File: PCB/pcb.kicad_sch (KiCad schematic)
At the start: 220 parts

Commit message: Added LEDs to the Schematic
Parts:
- added D? (x100): SK6812MINI, LED_SMD:LED_SK6812MINI_PLCC4_3.5x3.5mm_P1.75mm, symbol LED:SK6812MINI
- C1: value (none) -> 10u; footprint (none) -> Capacitor_SMD:C_0805_2012Metric
- C2, C3, C4: value (none) -> 0.1uF; footprint (none) -> Capacitor_SMD:C_0805_2012Metric
- C5, C6: value (none) -> 22pF; footprint (none) -> Capacitor_SMD:C_0805_2012Metric
- C7: value (none) -> 10uF; footprint (none) -> Capacitor_SMD:C_0805_2012Metric
- C8: value (none) -> 1uF; footprint (none) -> Capacitor_SMD:C_0805_2012Metric
- D1: value (none) -> Esc; footprint (none) -> Diode_SMD:D_SOD-123
- D10: value (none) -> <; footprint (none) -> Diode_SMD:D_SOD-123
- D100, D74: value (none) -> Enter; footprint (none) -> Diode_SMD:D_SOD-123
- D11, D71: value (none) -> Win; footprint (none) -> Diode_SMD:D_SOD-123
- D12: value (none) -> F1; footprint (none) -> Diode_SMD:D_SOD-123
- D13, D92: value (none) -> 2; footprint (none) -> Diode_SMD:D_SOD-123
- D14: value (none) -> W; footprint (none) -> Diode_SMD:D_SOD-123
- D15: value (none) -> S; footprint (none) -> Diode_SMD:D_SOD-123
- D16: value (none) -> Y; footprint (none) -> Diode_SMD:D_SOD-123
- D17: value (none) -> Alt; footprint (none) -> Diode_SMD:D_SOD-123
- D18: value (none) -> F2; footprint (none) -> Diode_SMD:D_SOD-123
- D19, D97: value (none) -> 3; footprint (none) -> Diode_SMD:D_SOD-123
- D2: value (none) -> ^; footprint (none) -> Diode_SMD:D_SOD-123
- D20: value (none) -> E; footprint (none) -> Diode_SMD:D_SOD-123
- D21: value (none) -> D; footprint (none) -> Diode_SMD:D_SOD-123
- D22: value (none) -> X; footprint (none) -> Diode_SMD:D_SOD-123
- D23: value (none) -> F3; footprint (none) -> Diode_SMD:D_SOD-123
- D24, D86: value (none) -> 4; footprint (none) -> Diode_SMD:D_SOD-123
- D25: value (none) -> R; footprint (none) -> Diode_SMD:D_SOD-123
- D26: value (none) -> F; footprint (none) -> Diode_SMD:D_SOD-123
- D27: value (none) -> C; footprint (none) -> Diode_SMD:D_SOD-123
- D28: value (none) -> F4; footprint (none) -> Diode_SMD:D_SOD-123
- D29, D91: value (none) -> 5; footprint (none) -> Diode_SMD:D_SOD-123
- D3: value (none) -> Tab; footprint (none) -> Diode_SMD:D_SOD-123
- D30: value (none) -> T; footprint (none) -> Diode_SMD:D_SOD-123
- D31: value (none) -> G; footprint (none) -> Diode_SMD:D_SOD-123
- D32: value (none) -> V; footprint (none) -> Diode_SMD:D_SOD-123
- D33: value (none) -> F5; footprint (none) -> Diode_SMD:D_SOD-123
- D34, D96: value (none) -> 6; footprint (none) -> Diode_SMD:D_SOD-123
- D35: value (none) -> Z; footprint (none) -> Diode_SMD:D_SOD-123
- D36: value (none) -> H; footprint (none) -> Diode_SMD:D_SOD-123
- D37: value (none) -> B; footprint (none) -> Diode_SMD:D_SOD-123
- D38: value (none) -> Leer; footprint (none) -> Diode_SMD:D_SOD-123
- D39: value (none) -> F6; footprint (none) -> Diode_SMD:D_SOD-123
- D4: value (none) -> Caps; footprint (none) -> Diode_SMD:D_SOD-123
- D40, D85: value (none) -> 7; footprint (none) -> Diode_SMD:D_SOD-123
- D41: value (none) -> U; footprint (none) -> Diode_SMD:D_SOD-123
- D42: value (none) -> J; footprint (none) -> Diode_SMD:D_SOD-123
- D43: value (none) -> N; footprint (none) -> Diode_SMD:D_SOD-123
- D44: value (none) -> F7; footprint (none) -> Diode_SMD:D_SOD-123
- D45, D90: value (none) -> 8; footprint (none) -> Diode_SMD:D_SOD-123
- D46: value (none) -> I; footprint (none) -> Diode_SMD:D_SOD-123
- D47: value (none) -> K; footprint (none) -> Diode_SMD:D_SOD-123
- D48: value (none) -> M; footprint (none) -> Diode_SMD:D_SOD-123
- D49: value (none) -> F8; footprint (none) -> Diode_SMD:D_SOD-123
- D5, D70: value (none) -> Shift; footprint (none) -> Diode_SMD:D_SOD-123
- D50, D95: value (none) -> 9; footprint (none) -> Diode_SMD:D_SOD-123
- D51: value (none) -> O; footprint (none) -> Diode_SMD:D_SOD-123
- D52: value (none) -> L; footprint (none) -> Diode_SMD:D_SOD-123
- D53, D93: value (none) -> ,; footprint (none) -> Diode_SMD:D_SOD-123
- D54: value (none) -> F9; footprint (none) -> Diode_SMD:D_SOD-123
- D55, D88: value (none) -> 0; footprint (none) -> Diode_SMD:D_SOD-123
- D56: value (none) -> P; footprint (none) -> Diode_SMD:D_SOD-123
- D57: value (none) -> Ö; footprint (none) -> Diode_SMD:D_SOD-123
- D58: value (none) -> .; footprint (none) -> Diode_SMD:D_SOD-123
- D59: value (none) -> AltGr; footprint (none) -> Diode_SMD:D_SOD-123
- D6: value (none) -> Ctrl; footprint (none) -> Diode_SMD:D_SOD-123
- D60: value (none) -> F10; footprint (none) -> Diode_SMD:D_SOD-123
- D61: value (none) -> ß; footprint (none) -> Diode_SMD:D_SOD-123
- D62: value (none) -> Ü; footprint (none) -> Diode_SMD:D_SOD-123
- D63: value (none) -> Ä; footprint (none) -> Diode_SMD:D_SOD-123
- D64, D98: value (none) -> -; footprint (none) -> Diode_SMD:D_SOD-123
- D65: value (none) -> Fn; footprint (none) -> Diode_SMD:D_SOD-123
- D66: value (none) -> F11; footprint (none) -> Diode_SMD:D_SOD-123
- D67: value (none) -> ´; footprint (none) -> Diode_SMD:D_SOD-123
- D68, D99: value (none) -> +; footprint (none) -> Diode_SMD:D_SOD-123
- D69: value (none) -> #; footprint (none) -> Diode_SMD:D_SOD-123
- D7, D87: value (none) -> 1; footprint (none) -> Diode_SMD:D_SOD-123
- D72: value (none) -> F12; footprint (none) -> Diode_SMD:D_SOD-123
- D73: value (none) -> Back; footprint (none) -> Diode_SMD:D_SOD-123
- D75: value (none) -> Left; footprint (none) -> Diode_SMD:D_SOD-123
- D76: value (none) -> Up; footprint (none) -> Diode_SMD:D_SOD-123
- D77: value (none) -> Down; footprint (none) -> Diode_SMD:D_SOD-123
- D78: value (none) -> Right; footprint (none) -> Diode_SMD:D_SOD-123
- D79: value (none) -> Druck; footprint (none) -> Diode_SMD:D_SOD-123
- D8: value (none) -> Q; footprint (none) -> Diode_SMD:D_SOD-123
- D80: value (none) -> Insert; footprint (none) -> Diode_SMD:D_SOD-123
- D81: value (none) -> Del; footprint (none) -> Diode_SMD:D_SOD-123
- D82: value (none) -> PgUp; footprint (none) -> Diode_SMD:D_SOD-123
- D83: value (none) -> PgDn; footprint (none) -> Diode_SMD:D_SOD-123
- D84: value (none) -> NumLock; footprint (none) -> Diode_SMD:D_SOD-123
- D89: value (none) -> /; footprint (none) -> Diode_SMD:D_SOD-123
- D9: value (none) -> A; footprint (none) -> Diode_SMD:D_SOD-123
- D94: value (none) -> *; footprint (none) -> Diode_SMD:D_SOD-123
- F1: value (none) -> 500mA; footprint (none) -> Fuse:Fuse_1206_3216Metric
- FB1: value (none) -> 600R; footprint (none) -> Ferrite_THT:LairdTech_28C0236-0JW-10
- J1: value (none) -> USB_C_Receptacle_USB2.0; footprint (none) -> Connector_USB:USB_C_Receptacle_HRO_TYPE-C-31-M-12
- MX? (x100): value (none) -> MX-NoLED
- R1, R2: value (none) -> 5K1; footprint (none) -> Resistor_SMD:R_0805_2012Metric
- R3, R4: value (none) -> 22; footprint (none) -> Resistor_SMD:R_0805_2012Metric
- R5, R6: value (none) -> 10k; footprint (none) -> Resistor_SMD:R_0805_2012Metric
- SW1: value (none) -> SW_Push; footprint (none) -> random-keyboard-parts:SKQG-1155865
- U1: value (none) -> AT90USB1286-AU; footprint (none) -> Package_QFP:TQFP-64_14x14mm_P0.8mm
- Y1: value (none) -> Crystal_GND24_Small; footprint (none) -> Crystal:Crystal_SMD_3225-4Pin_3.2x2.5mm
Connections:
- net +5V: now also D?.4 (VDD), D?.4 (VDD), D?.4 (VDD), D?.4 (VDD), D?.4 (VDD), D?.4 (VDD), D?.4 (VDD), D?.4 (VDD), D?.4 (VDD), D?.4 (VDD), D?.4 (VDD), D?.4 (VDD), D?.4 (VDD), D?.4 (VDD), D?.4 (VDD), D?.4 (VDD), D?.4 (VDD), D?.4 (VDD), D?.4 (VDD), D?.4 (VDD), D?.4 (VDD), D?.4 (VDD), D?.4 (VDD), D?.4 (VDD), D?.4 (VDD), D?.4 (VDD), D?.4 (VDD), D?.4 (VDD), D?.4 (VDD), D?.4 (VDD), D?.4 (VDD), D?.4 (VDD), D?.4 (VDD), D?.4 (VDD), D?.4 (VDD), D?.4 (VDD), D?.4 (VDD), D?.4 (VDD), D?.4 (VDD), D?.4 (VDD), D?.4 (VDD), D?.4 (VDD), D?.4 (VDD), D?.4 (VDD), D?.4 (VDD), D?.4 (VDD), D?.4 (VDD), D?.4 (VDD), D?.4 (VDD), D?.4 (VDD), D?.4 (VDD), D?.4 (VDD), D?.4 (VDD), D?.4 (VDD), D?.4 (VDD), D?.4 (VDD), D?.4 (VDD), D?.4 (VDD), D?.4 (VDD), D?.4 (VDD), D?.4 (VDD), D?.4 (VDD), D?.4 (VDD), D?.4 (VDD), D?.4 (VDD), D?.4 (VDD), D?.4 (VDD), D?.4 (VDD), D?.4 (VDD), D?.4 (VDD), D?.4 (VDD), D?.4 (VDD), D?.4 (VDD), D?.4 (VDD), D?.4 (VDD), D?.4 (VDD), D?.4 (VDD), D?.4 (VDD), D?.4 (VDD), D?.4 (VDD), D?.4 (VDD), D?.4 (VDD), D?.4 (VDD), D?.4 (VDD), D?.4 (VDD), D?.4 (VDD), D?.4 (VDD), D?.4 (VDD), D?.4 (VDD), D?.4 (VDD), D?.4 (VDD), D?.4 (VDD), D?.4 (VDD), D?.4 (VDD), D?.4 (VDD), D?.4 (VDD), D?.4 (VDD), D?.4 (VDD), D?.4 (VDD), D?.4 (VDD)
- net GND: now also D?.2 (VSS), D?.2 (VSS), D?.2 (VSS), D?.2 (VSS), D?.2 (VSS), D?.2 (VSS), D?.2 (VSS), D?.2 (VSS), D?.2 (VSS), D?.2 (VSS), D?.2 (VSS), D?.2 (VSS), D?.2 (VSS), D?.2 (VSS), D?.2 (VSS), D?.2 (VSS), D?.2 (VSS), D?.2 (VSS), D?.2 (VSS), D?.2 (VSS), D?.2 (VSS), D?.2 (VSS), D?.2 (VSS), D?.2 (VSS), D?.2 (VSS), D?.2 (VSS), D?.2 (VSS), D?.2 (VSS), D?.2 (VSS), D?.2 (VSS), D?.2 (VSS), D?.2 (VSS), D?.2 (VSS), D?.2 (VSS), D?.2 (VSS), D?.2 (VSS), D?.2 (VSS), D?.2 (VSS), D?.2 (VSS), D?.2 (VSS), D?.2 (VSS), D?.2 (VSS), D?.2 (VSS), D?.2 (VSS), D?.2 (VSS), D?.2 (VSS), D?.2 (VSS), D?.2 (VSS), D?.2 (VSS), D?.2 (VSS), D?.2 (VSS), D?.2 (VSS), D?.2 (VSS), D?.2 (VSS), D?.2 (VSS), D?.2 (VSS), D?.2 (VSS), D?.2 (VSS), D?.2 (VSS), D?.2 (VSS), D?.2 (VSS), D?.2 (VSS), D?.2 (VSS), D?.2 (VSS), D?.2 (VSS), D?.2 (VSS), D?.2 (VSS), D?.2 (VSS), D?.2 (VSS), D?.2 (VSS), D?.2 (VSS), D?.2 (VSS), D?.2 (VSS), D?.2 (VSS), D?.2 (VSS), D?.2 (VSS), D?.2 (VSS), D?.2 (VSS), D?.2 (VSS), D?.2 (VSS), D?.2 (VSS), D?.2 (VSS), D?.2 (VSS), D?.2 (VSS), D?.2 (VSS), D?.2 (VSS), D?.2 (VSS), D?.2 (VSS), D?.2 (VSS), D?.2 (VSS), D?.2 (VSS), D?.2 (VSS), D?.2 (VSS), D?.2 (VSS), D?.2 (VSS), D?.2 (VSS), D?.2 (VSS), D?.2 (VSS), D?.2 (VSS), D?.2 (VSS)
- new net: D?.1 (DOUT), D?.3 (DIN) (x90)
- new net RGBDIN: D?.3 (DIN)
- new net RGBDOUT0: D?.1 (DOUT), D?.3 (DIN)
- new net RGBDOUT1: D?.1 (DOUT), D?.3 (DIN)
- new net RGBDOUT2: D?.1 (DOUT), D?.3 (DIN)
- new net RGBDOUT3: D?.1 (DOUT), D?.3 (DIN)
- new net RGBDOUT4: D?.1 (DOUT), D?.3 (DIN)
- new net RGBDOUT5: D?.1 (DOUT), D?.3 (DIN)
- new net RGBDOUT6: D?.1 (DOUT), D?.3 (DIN)
- new net RGBDOUT7: D?.1 (DOUT), D?.3 (DIN)
- new net RGBDOUT8: D?.1 (DOUT), D?.3 (DIN)
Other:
- company: (none) -> DiomKBS
- title: (none) -> Diom-75TK
- moved on the sheet: D1, D10, D100, D11, D12, D13, D14, D15, D16, D17, D18, D19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

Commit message: Submodule, LEDs, Footprints
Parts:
- MX1, MX10, MX12, MX13, MX14, MX15, MX16, MX18, MX19, MX2, MX20, MX21, MX22, MX23, MX24, MX25, MX26, MX27, MX28, MX29, MX30, MX31, MX32, MX33, MX34, MX35, MX36, MX37, MX39, MX40, MX41, MX42, MX43, MX44, MX45, MX46, MX47, MX48, MX49, MX50, MX51, MX52, MX53, MX54, MX55, MX56, MX57, MX58, MX60, MX61, MX62, MX63, MX64, MX65, MX66, MX67, MX68, MX69, MX7, MX71, MX72, MX75, MX76, MX77, MX78, MX79, MX8, MX80, MX81, MX82, MX83, MX84, MX85, MX86, MX87, MX89, MX9, MX90, MX91, MX92, MX93, MX94, MX95, MX96, MX97, MX98: renamed from MX?; footprint (none) -> MX_Alps_Hybrid:MX-1U-NoLED
- MX11, MX17, MX5, MX59, MX6: renamed from MX?; footprint (none) -> MX_Alps_Hybrid:MX-1.25U-NoLED
- MX3: renamed from MX?; footprint (none) -> MX_Alps_Hybrid:MX-1.5U-NoLED
- MX38: renamed from MX?; footprint (none) -> MX_Alps_Hybrid:MX-6U-Centered-NoLED
- MX4, MX70: renamed from MX?; footprint (none) -> MX_Alps_Hybrid:MX-1.75U-NoLED
- MX73, MX88: renamed from MX?; footprint (none) -> MX_Alps_Hybrid:MX-2U-NoLED
- gave numbers to parts that had none: 103

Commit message: Started PCB + Changed Footprints
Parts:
- D101, D102, D103, D104, D105, D106, D107, D108, D109, D110, D111, D112, D113, D114, D115, D116, D117, D118, D119, D120, D121, D122, D123, D124, D125, D126, D127, D128, D129, D130, D131, D132, D133, D134, D135, D136, D137, D138, D139, D140, D141, D142, D143, D144, D145, D146, D147, D148, D149, D150, D151, D152, D153, D154, D155, D156, D157, D158, D159, D160, D161, D162, D163, D164, D165, D166, D167, D168, D169, D170, D171, D172, D173, D174, D175, D176, D177, D178, D179, D180, D181, D182, D183, D184, D185, D186, D187, D188, D189, D190, D191, D192, D193, D194, D195, D196, D197, D198, D199, D200: footprint LED_SMD:LED_SK6812MINI_PLCC4_3.5x3.5mm_P1.75mm -> (none)
- MX1, MX10, MX12, MX13, MX14, MX15, MX16, MX18, MX19, MX2, MX20, MX21, MX22, MX23, MX24, MX25, MX26, MX27, MX28, MX29, MX30, MX31, MX32, MX33, MX34, MX35, MX36, MX37, MX39, MX40, MX41, MX42, MX43, MX44, MX45, MX46, MX47, MX48, MX49, MX50, MX51, MX52, MX53, MX54, MX55, MX56, MX57, MX58, MX60, MX61, MX62, MX63, MX64, MX65, MX66, MX67, MX68, MX69, MX7, MX71, MX72, MX75, MX76, MX77, MX78, MX79, MX8, MX80, MX81, MX82, MX83, MX84, MX85, MX86, MX87, MX89, MX9, MX90, MX91, MX92, MX93, MX94, MX95, MX96, MX97, MX98: footprint MX_Alps_Hybrid:MX-1U-NoLED -> (none)
- MX11, MX17, MX5, MX59, MX6: footprint MX_Alps_Hybrid:MX-1.25U-NoLED -> (none)
- MX3: footprint MX_Alps_Hybrid:MX-1.5U-NoLED -> (none)
- MX38: footprint MX_Alps_Hybrid:MX-6U-Centered-NoLED -> (none)
- MX4, MX70: footprint MX_Alps_Hybrid:MX-1.75U-NoLED -> (none)
- MX73, MX88: footprint MX_Alps_Hybrid:MX-2U-NoLED -> (none)

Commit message: Finished Switch Layout
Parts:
- D101, D102, D103, D104, D105, D106, D107, D108, D109, D110, D111, D112, D113, D114, D115, D116, D117, D118, D119, D120, D121, D122, D123, D124, D125, D126, D127, D128, D129, D130, D131, D132, D133, D134, D135, D136, D137, D138, D139, D140, D141, D142, D143, D144, D145, D146, D147, D148, D149, D150, D151, D152, D153, D154, D155, D156, D157, D158, D159, D160, D161, D162, D163, D164, D165, D166, D167, D168, D169, D170, D171, D172, D173, D174, D175, D176, D177, D178, D179, D180, D181, D182, D183, D184, D185, D186, D187, D188, D189, D190, D191, D192, D193, D194, D195, D196, D197, D198, D199, D200: footprint (none) -> led:SK6812MINI_3.5x3.7mm_SMD
- MX1, MX10, MX12, MX13, MX14, MX15, MX16, MX18, MX19, MX2, MX20, MX21, MX22, MX23, MX24, MX25, MX26, MX27, MX28, MX29, MX30, MX31, MX32, MX33, MX34, MX35, MX36, MX37, MX39, MX40, MX41, MX42, MX43, MX44, MX45, MX46, MX47, MX48, MX49, MX50, MX51, MX52, MX53, MX54, MX55, MX56, MX57, MX58, MX60, MX61, MX62, MX63, MX64, MX65, MX66, MX67, MX68, MX69, MX7, MX71, MX72, MX75, MX76, MX77, MX78, MX79, MX8, MX80, MX81, MX82, MX83, MX84, MX85, MX86, MX87, MX89, MX9, MX90, MX91, MX92, MX93, MX94, MX95, MX96, MX97, MX98: footprint (none) -> kailh-switches-hotswap:Kailh-Hotswap-1U
- MX100, MX99: footprint (none) -> kailh-switches-hotswap:Kailh-Hotswap-2U-Vertical
- MX11, MX17, MX5, MX59, MX6: footprint (none) -> kailh-switches-hotswap:Kailh-Hotswap-1.25U
- MX3: footprint (none) -> kailh-switches-hotswap:Kailh-Hotswap-1.5U
- MX38: footprint (none) -> kailh-switches-hotswap:Kailh-Hotswap-6U
- MX4: footprint (none) -> kailh-switches-hotswap:Kailh-Hotswap-1.75U
- MX73, MX88: footprint (none) -> kailh-switches-hotswap:Kailh-Hotswap-2U
- MX74: footprint (none) -> kailh-switches-hotswap:Kailh-Hotswap-EnterISO

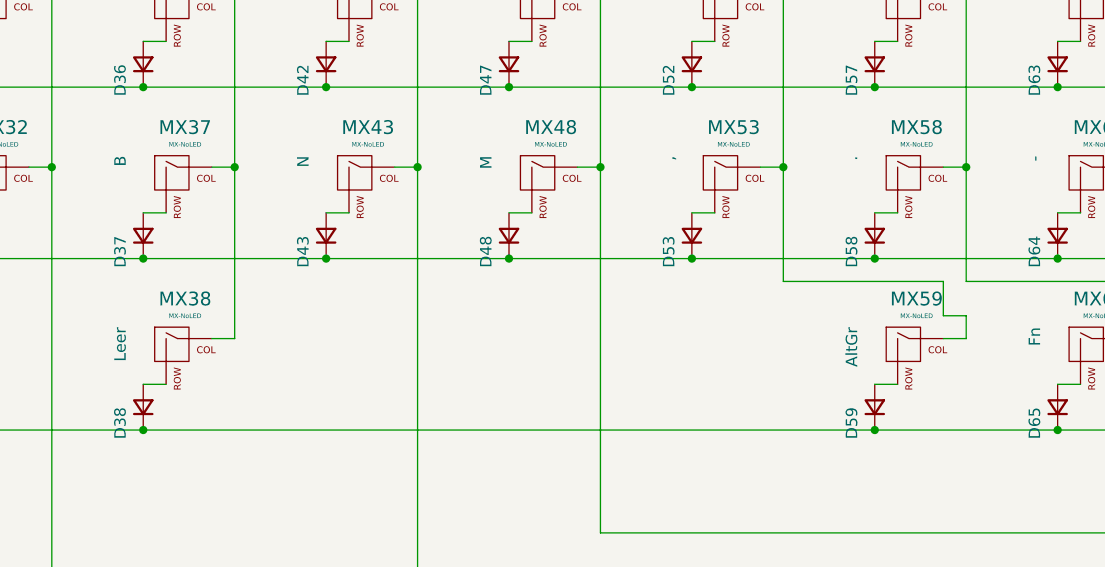
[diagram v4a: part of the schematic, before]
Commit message: Diode placement, Alternative Bottom Rows
-New Footprints
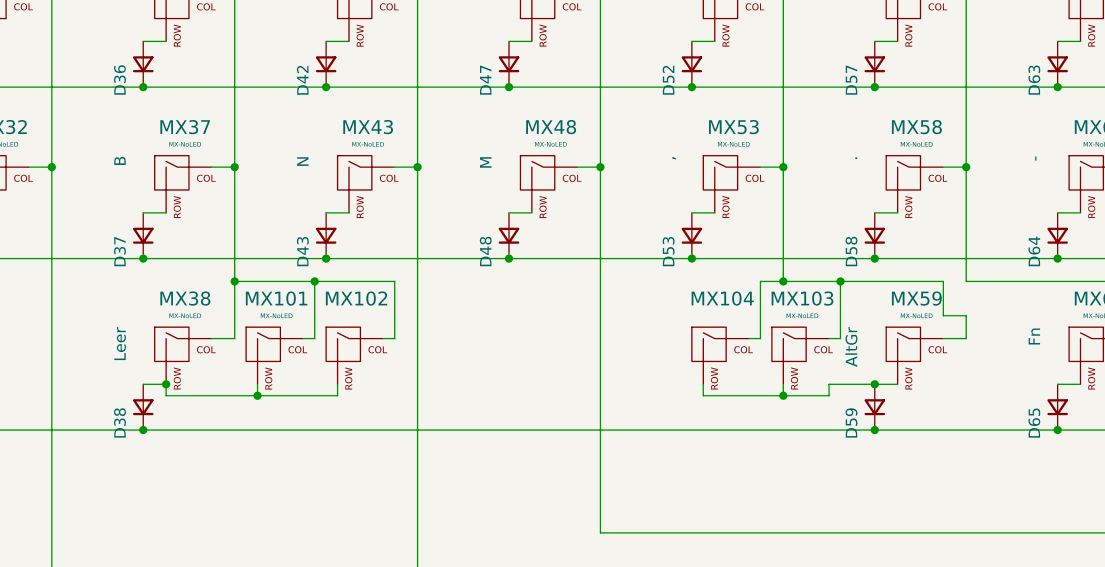
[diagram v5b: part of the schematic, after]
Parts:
- added MX101, MX103: MX-NoLED, symbol pcb-rescue:MX-NoLED-MX_Alps_Hybrid
- added MX102, MX104: (no value), symbol pcb-rescue:MX-NoLED-MX_Alps_Hybrid
- MX1, MX10, MX12, MX13, MX14, MX15, MX16, MX18, MX19, MX2, MX20, MX21, MX22, MX23, MX24, MX25, MX26, MX27, MX28, MX29, MX30, MX31, MX32, MX33, MX34, MX35, MX36, MX37, MX39, MX40, MX41, MX42, MX43, MX44, MX45, MX46, MX47, MX48, MX49, MX50, MX51, MX52, MX53, MX54, MX55, MX56, MX57, MX58, MX60, MX61, MX62, MX63, MX64, MX65, MX66, MX67, MX68, MX69, MX7, MX71, MX72, MX75, MX76, MX77, MX78, MX79, MX8, MX80, MX81, MX82, MX83, MX84, MX85, MX86, MX87, MX89, MX9, MX90, MX91, MX92, MX93, MX94, MX95, MX96, MX97, MX98: footprint kailh-switches-hotswap:Kailh-Hotswap-1U -> (none)
- MX100, MX99: footprint kailh-switches-hotswap:Kailh-Hotswap-2U-Vertical -> (none)
- MX11, MX17, MX5, MX59, MX6: footprint kailh-switches-hotswap:Kailh-Hotswap-1.25U -> (none)
- MX3: footprint kailh-switches-hotswap:Kailh-Hotswap-1.5U -> (none)
- MX38: footprint kailh-switches-hotswap:Kailh-Hotswap-6U -> (none)
- MX4: footprint kailh-switches-hotswap:Kailh-Hotswap-1.75U -> (none)
- MX73, MX88: footprint kailh-switches-hotswap:Kailh-Hotswap-2U -> (none)
- MX74: footprint kailh-switches-hotswap:Kailh-Hotswap-EnterISO -> (none)
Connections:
- net COL6: now also MX101.1 (COL), MX102.1 (COL)
- net COL9: now also MX103.1 (COL), MX104.1 (COL)
- net at D59.2 (A), MX59.2 (ROW): now also MX103.2 (ROW), MX104.2 (ROW)
- net at D38.2 (A), MX38.2 (ROW): now also MX101.2 (ROW), MX102.2 (ROW)

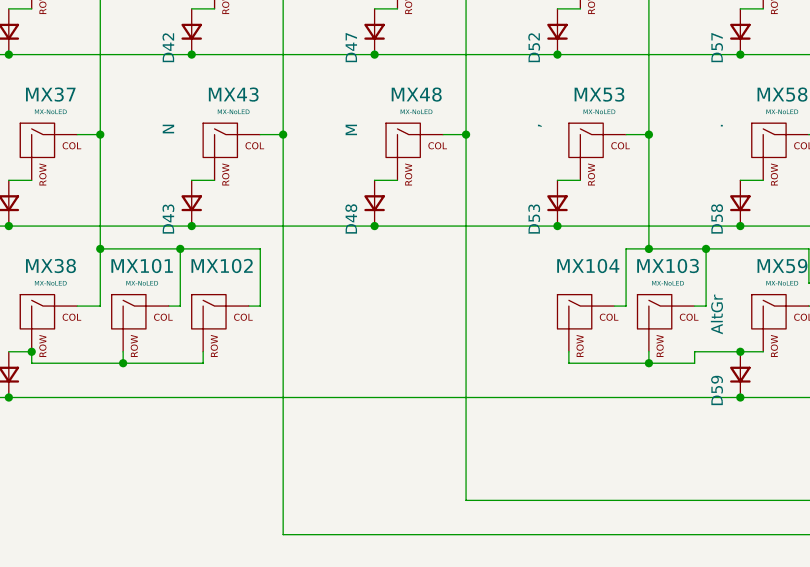
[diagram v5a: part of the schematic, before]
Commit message: Changed Footprint for Ferrite
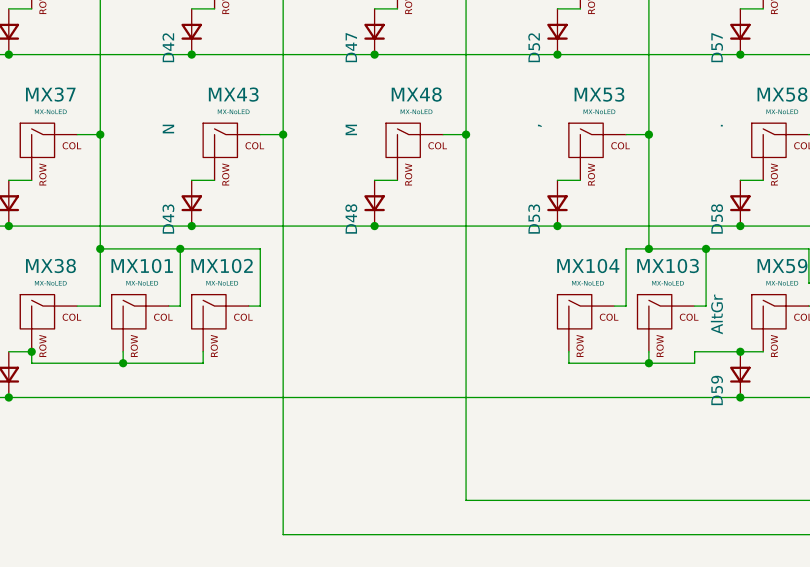
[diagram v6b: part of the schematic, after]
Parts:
- FB1: footprint Ferrite_THT:LairdTech_28C0236-0JW-10 -> (none)
- MX1, MX10, MX103, MX11, MX12, MX13, MX14, MX15, MX16, MX18, MX19, MX2, MX20, MX21, MX22, MX23, MX24, MX25, MX26, MX27, MX28, MX29, MX30, MX31, MX32, MX33, MX34, MX35, MX36, MX37, MX39, MX40, MX41, MX42, MX43, MX44, MX45, MX46, MX47, MX48, MX49, MX50, MX51, MX52, MX53, MX54, MX55, MX56, MX57, MX58, MX60, MX61, MX62, MX63, MX64, MX65, MX66, MX67, MX68, MX69, MX7, MX71, MX72, MX75, MX76, MX77, MX78, MX79, MX8, MX81, MX82, MX83, MX84, MX85, MX86, MX87, MX88, MX89, MX9, MX90, MX91, MX92, MX93, MX94, MX95, MX96, MX97, MX98: footprint (none) -> kailh-switches-hotswap:Kailh-Hotswap-1U
- MX100, MX99: footprint (none) -> kailh-switches-hotswap:Kailh-Hotswap-2U-Vertical
- MX101: footprint (none) -> kailh-switches-hotswap:Kailh-Hotswap-6.25U
- MX102: value (none) -> MX-NoLED; footprint (none) -> kailh-switches-hotswap:Kailh-Hotswap-7U
- MX104: value (none) -> MX-NoLED; footprint (none) -> kailh-switches-hotswap:Kailh-Hotswap-1.25U
- MX17, MX5, MX59: footprint (none) -> kailh-switches-hotswap:Kailh-Hotswap-1.25U
- MX3, MX6: footprint (none) -> kailh-switches-hotswap:Kailh-Hotswap-1.5U
- MX38: footprint (none) -> kailh-switches-hotswap:Kailh-Hotswap-6U
- MX4, MX70: footprint (none) -> kailh-switches-hotswap:Kailh-Hotswap-1.75U
- MX73, MX80: footprint (none) -> kailh-switches-hotswap:Kailh-Hotswap-2U
- MX74: footprint (none) -> kailh-switches-hotswap:Kailh-Hotswap-EnterISO

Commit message: Placed all LEDs
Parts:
- FB1: footprint (none) -> josh-passives-smt:Ferrite_Bead_0603
- MX80: footprint kailh-switches-hotswap:Kailh-Hotswap-2U -> (none)
- MX88: footprint kailh-switches-hotswap:Kailh-Hotswap-1U -> (none)
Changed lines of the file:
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@@
     (property "Reference" "FB1" (id 0) (at 81.28 38.4302 90))
     (property "Value" "600R" (id 1) (at 81.28 40.7416 90))
-    (property "Footprint" "" (id 2) (at 81.28 42.672 90)
+    (property "Footprint" "josh-passives-smt:Ferrite_Bead_0603" (id 2) (at 81.28 42.672 90)
       (effects (font (size 1.27 1.27)) hide)
     )
@@
       (effects (font (size 0.508 0.508)))
     )
-    (property "Footprint" "kailh-switches-hotswap:Kailh-Hotswap-2U" (id 2) (at 525.145 62.865 0)
+    (property "Footprint" "" (id 2) (at 525.145 62.865 0)
       (effects (font (size 1.524 1.524)) hide)
     )
@@
       (effects (font (size 0.508 0.508)))
     )
-    (property "Footprint" "kailh-switches-hotswap:Kailh-Hotswap-1U" (id 2) (at 558.165 139.065 0)
+    (property "Footprint" "" (id 2) (at 558.165 139.065 0)
       (effects (font (size 1.524 1.524)) hide)
     )
@@
     )
     (path "/00000000-0000-0000-0000-00006266e6bf"
-      (reference "MX80") (unit 1) (value "MX-NoLED") (footprint "kailh-switches-hotswap:Kailh-Hotswap-2U")
+      (reference "MX80") (unit 1) (value "MX-NoLED") (footprint "kailh-switches-hotswap:Kailh-Hotswap-1U")
     )
     (path "/00000000-0000-0000-0000-00006267a4e1"
@@
     )
     (path "/00000000-0000-0000-0000-00006268f908"
-      (reference "MX88") (unit 1) (value "MX-NoLED") (footprint "kailh-switches-hotswap:Kailh-Hotswap-1U")
+      (reference "MX88") (unit 1) (value "MX-NoLED") (footprint "kailh-switches-hotswap:Kailh-Hotswap-2U")
     )
     (path "/00000000-0000-0000-0000-00006266dd7b"

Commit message: PCB Size, LED Footprints
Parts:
- D1, D10, D100, D11, D12, D13, D14, D15, D16, D17, D18, D19, D2, D20, D21, D22, D23, D24, D25, D26, D27, D28, D29, D3, D30, D31, D32, D33, D34, D35, D36, D37, D38, D39, D4, D40, D41, D42, D43, D44, D45, D46, D47, D48, D49, D5, D50, D51, D52, D53, D54, D55, D56, D57, D58, D59, D6, D60, D61, D62, D63, D64, D65, D66, D67, D68, D69, D7, D70, D71, D72, D73, D74, D75, D76, D77, D78, D79, D8, D80, D81, D82, D83, D84, D85, D86, D87, D88, D89, D9, D90, D91, D92, D93, D94, D95, D96, D97, D98, D99: footprint Diode_SMD:D_SOD-123 -> (none)
- D101, D102, D103, D104, D105, D106, D107, D108, D109, D110, D111, D112, D113, D114, D115, D116, D117, D118, D119, D120, D121, D122, D123, D124, D125, D126, D127, D128, D129, D130, D131, D132, D133, D134, D135, D136, D137, D138, D139, D140, D141, D142, D143, D144, D145, D146, D147, D148, D149, D150, D151, D152, D153, D154, D155, D156, D157, D158, D159, D160, D161, D162, D163, D164, D165, D166, D167, D168, D169, D170, D171, D172, D173, D174, D175, D176, D177, D178, D179, D180, D181, D182, D183, D184, D185, D186, D187, D188, D189, D190, D191, D192, D193, D194, D195, D196, D197, D198, D199, D200: footprint led:SK6812MINI_3.5x3.7mm_SMD -> (none)
- MX80: footprint (none) -> kailh-switches-hotswap:Kailh-Hotswap-1U
- MX88: footprint (none) -> kailh-switches-hotswap:Kailh-Hotswap-2U
